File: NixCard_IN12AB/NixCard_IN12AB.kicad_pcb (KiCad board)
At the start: 2 copper layers, 21.6 x 31.8 mm, 13 parts, among them P1 CONN_01X06, P2 CONN_01X06, P3 TSW-104-07-F-S, P4 TSW-104-07-F-S, U1 HV513WG, U2 HV513WG

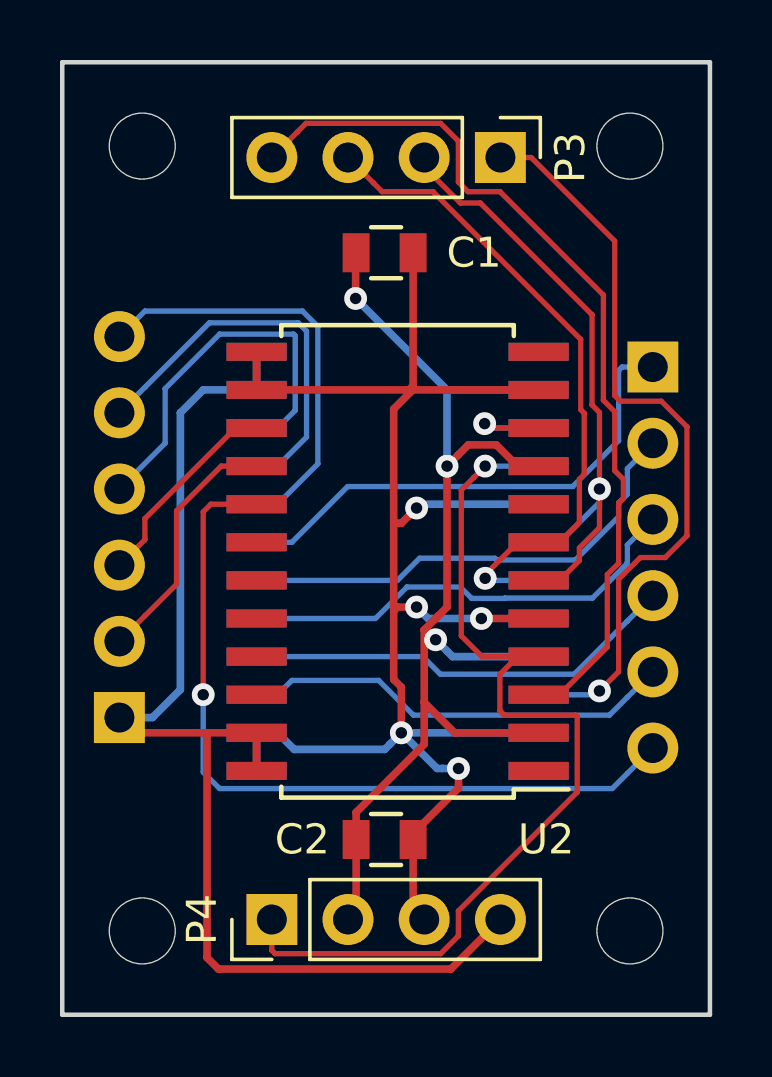
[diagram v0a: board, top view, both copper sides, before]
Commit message: Corrects names (driver <-> IN12AB)
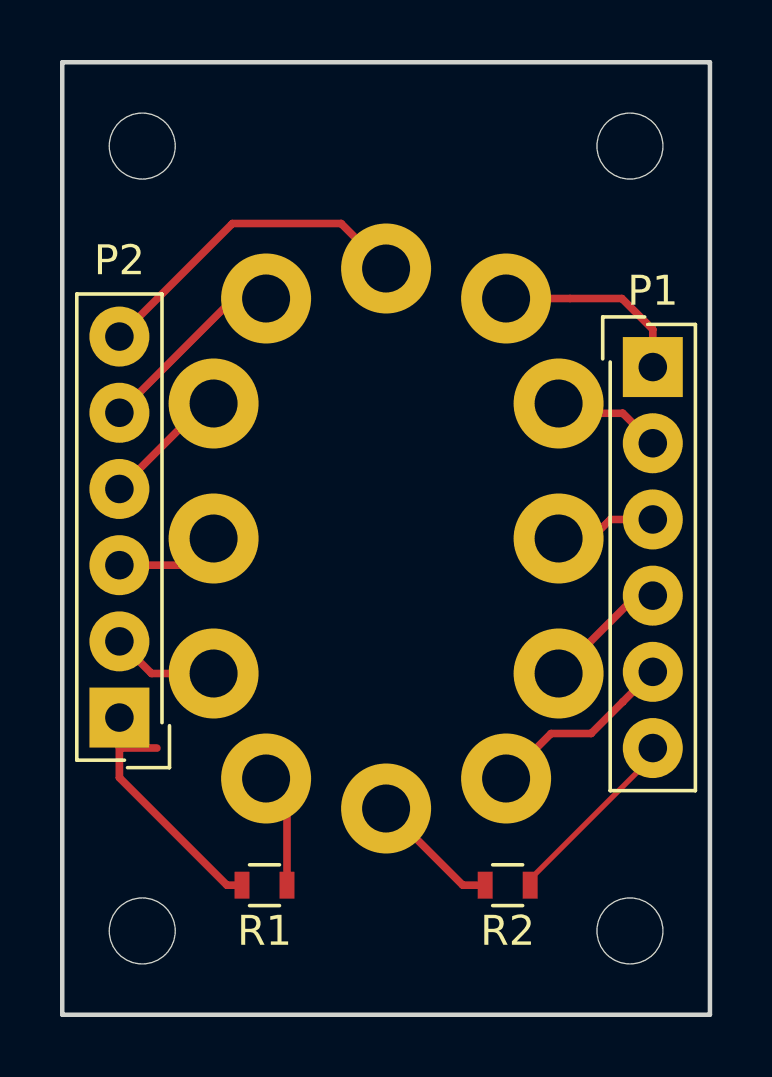
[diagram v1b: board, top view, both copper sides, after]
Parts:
- removed C1: 1u, quad_level_shifter:C_0805
- removed C2: 100n, quad_level_shifter:C_0805
- removed P3, P4: TSW-104-07-F-S, Pin_Headers:Pin_Header_Straight_1x04_Pitch2.54mm
- removed U1, U2: HV513WG, Package_SOIC:SOIC-24W_7.5x15.4mm_P1.27mm
- removed svg2mod: G***, footprints:oshw-logo-gear
- added N1: IN-12B, footprints:IN-12B-skt, B.Cu at (148.6, 104.8)
- added R1: 20k, Resistors_SMD:R_0603, F.Cu at (144.5, 116.3)
- added R2: 56k, Resistors_SMD:R_0603, F.Cu at (152.6, 116.3)
- added REF***: OSHW-Logo_5.7x6mm_SilkScreen, Symbols:OSHW-Logo_5.7x6mm_SilkScreen, B.Cu at (148.6, 108.0)
- P1, P2: footprint Pin_Headers:Pin_Header_Straight_1x06_Pitch2.54mm -> Connectors_Samtec:SL-106-X-XX_1x06; moved to F.Cu
- turned P1 to 0 degrees
- turned P2 to 180 degrees
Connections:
- P1 pad 1: /NIX5 -> Net-(N1-Pad5)
- P1 pad 2: /NIX4 -> Net-(N1-Pad4)
- P1 pad 3: /NIX3 -> Net-(N1-Pad3)
- P1 pad 4: /NIX2 -> Net-(N1-Pad2)
- P1 pad 5: /NIX1 -> Net-(N1-Pad1)
- P1 pad 6: /NIXDP -> Net-(P1-Pad6)
- P2 pad 2: /NIX0 -> Net-(N1-Pad0)
- P2 pad 3: /NIX9 -> Net-(N1-Pad9)
- P2 pad 4: /NIX8 -> Net-(N1-Pad8)
- P2 pad 5: /NIX7 -> Net-(N1-Pad7)
- P2 pad 6: /NIX6 -> Net-(N1-Pad6)
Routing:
- net GNDREF: track 56.6 -> 0.00 mm, vias 5 -> 0
- net +5V: track 40.0 -> 0.00 mm, vias 3 -> 0
- net /~OE: track 32.5 -> 0.00 mm, vias 1 -> 0
- net VAA: track 39.9 -> 7.58 mm
- net /DOUT: track 29.9 -> 0.00 mm
- net /NIXDP: track 26.3 -> 0.00 mm, vias 1 -> 0
- net /DIN: track 25.5 -> 0.00 mm, vias 1 -> 0
- net /~LE: track 22.3 -> 0.00 mm, vias 1 -> 0
- net /CLK: track 21.8 -> 0.00 mm, vias 1 -> 0
- net /NIX5: track 17.0 -> 0.00 mm
- net /NIX4: track 15.9 -> 0.00 mm
- net /NIX3: track 15.2 -> 0.00 mm
- net /NIX6: track 15.1 -> 0.00 mm
- net /NIX2: track 14.5 -> 0.00 mm
- net /NIX1: track 14.5 -> 0.00 mm
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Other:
- board text added: "BRD A REV C 2017 DEC 2"
- board text added: "THIS END UP"
- board text added: "USE 2-56 OR M2 SCREWS"
- board text added: "github.com/ RobertBaruch/NixCard"
- board text removed: "+170V"
- board text removed: "+5V"
- board text removed: "BRD B REV C 2017 DEC 2"
- board text removed: "CLK"
- board text removed: "DIN"
- board text removed: "DOUT"
- board text removed: "GND"
- board text removed: "S P"
- board text removed: "github.com/RobertBaruch/NixCard"
- board text removed: "~LE"
- board text removed: "~OE"

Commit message: Initial IN-12AB board, gerbers
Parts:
- removed P1, P2: CONN_01X06, Connectors_Samtec:SL-106-X-XX_1x06
- removed REF***: OSHW-Logo_5.7x6mm_SilkScreen, Symbols:OSHW-Logo_5.7x6mm_SilkScreen
- added P4: CONN_01X05, Pin_Headers:Pin_Header_Straight_1x05_Pitch2.54mm, F.Cu at (-5.08, -14.6)
- added P5: CONN_01X05, Pin_Headers:Pin_Header_Straight_1x05_Pitch2.54mm, F.Cu at (-9.53, 5.08)
- added P6: CONN_01X05, Pin_Headers:Pin_Header_Straight_1x05_Pitch2.54mm, F.Cu at (-5.08, 14.6)
- added P7: CONN_01X05, Pin_Headers:Pin_Header_Straight_1x05_Pitch2.54mm, F.Cu at (9.53, 3.81)
- added R10: 20k, Resistors_SMD:R_0603, F.Cu at (-2.78, 0.38)
- added R11: 20k, Resistors_SMD:R_0603, F.Cu at (-2.78, 2.41)
- added R3: 20k, Resistors_SMD:R_0603, F.Cu at (2.78, 2.79)
- added R4: 20k, Resistors_SMD:R_0603, F.Cu at (2.78, -0.13)
- added R5: 20k, Resistors_SMD:R_0603, F.Cu at (2.81, -3.17)
- added R6: 20k, Resistors_SMD:R_0603, F.Cu at (2.40, -11.3)
- added R7: 20k, Resistors_SMD:R_0603, F.Cu at (-0.13, -5.98)
- added R8: 20k, Resistors_SMD:R_0603, F.Cu at (-3.16, -10.5)
- added R9: 20k, Resistors_SMD:R_0603, F.Cu at (-2.78, -2.67)
- added svg2mod: G***, footprints:oshw-logo-gear, B.Cu at (6.93, -9.65)
- R1: value 20k -> 120k
- R2: value 56k -> 20k
- moved R2 187.2 mm to (1.64, 5.71), turned to 180 degrees
- moved N1 181.8 mm to (0.00, 0.00)
- moved REF** 181.8 mm to (8.13, 13.1)
- moved REF** 181.8 mm to (8.13, -13.1)
- moved REF** 181.8 mm to (-8.13, -13.1)
- moved REF** 181.8 mm to (-8.13, 13.1)
- moved R1 176.8 mm to (2.42, 11.2)
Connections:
- N1 pad A: Net-(N1-PadA) -> VAA
- R1 pad 1: VAA -> Net-(N1-PadLHDP)
- R1 pad 2: Net-(N1-PadA) -> /HV10
- R2 pad 1: Net-(N1-PadLHDP) -> Net-(N1-Pad1)
- R2 pad 2: Net-(P1-Pad6) -> /HV1
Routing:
- net VAA: track 7.58 -> 36.7 mm, vias 0 -> 1
- net GNDREF: track 0.00 -> 27.0 mm
- net /HV5: track 0.00 -> 22.9 mm
- net /HV4: track 0.00 -> 17.4 mm
- net /HV2: track 0.00 -> 14.7 mm
- net /HV1: track 0.00 -> 14.0 mm
- net /HV3: track 0.00 -> 13.7 mm
- net /HV9: track 0.00 -> 13.2 mm
- net /HV10: track 0.00 -> 12.8 mm
- net /HV6: track 0.00 -> 12.7 mm
- net /HV8: track 0.00 -> 12.2 mm
- net Net-(N1-Pad6): track 11.1 -> 2.32 mm
- net /HV7: track 0.00 -> 6.64 mm
- net Net-(P1-Pad6): track 6.27 -> 0.00 mm
- net /HV0: track 0.00 -> 6.05 mm
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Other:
- board text added: "IN-12AB REV C 2017 DEC 10"
- board text added: "S P"
- board text removed: "BRD A REV C 2017 DEC 2"
